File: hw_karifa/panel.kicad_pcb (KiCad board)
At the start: 2 copper layers, 141.8 x 210.4 mm, 763 parts, among them J1 Conn_2Rows-05Pins, Q1 AO3401A, Q2 AO3401A, Q3 AO3401A, SW1 SW_DPST_x2, U1 PY32F002AF15P6TU

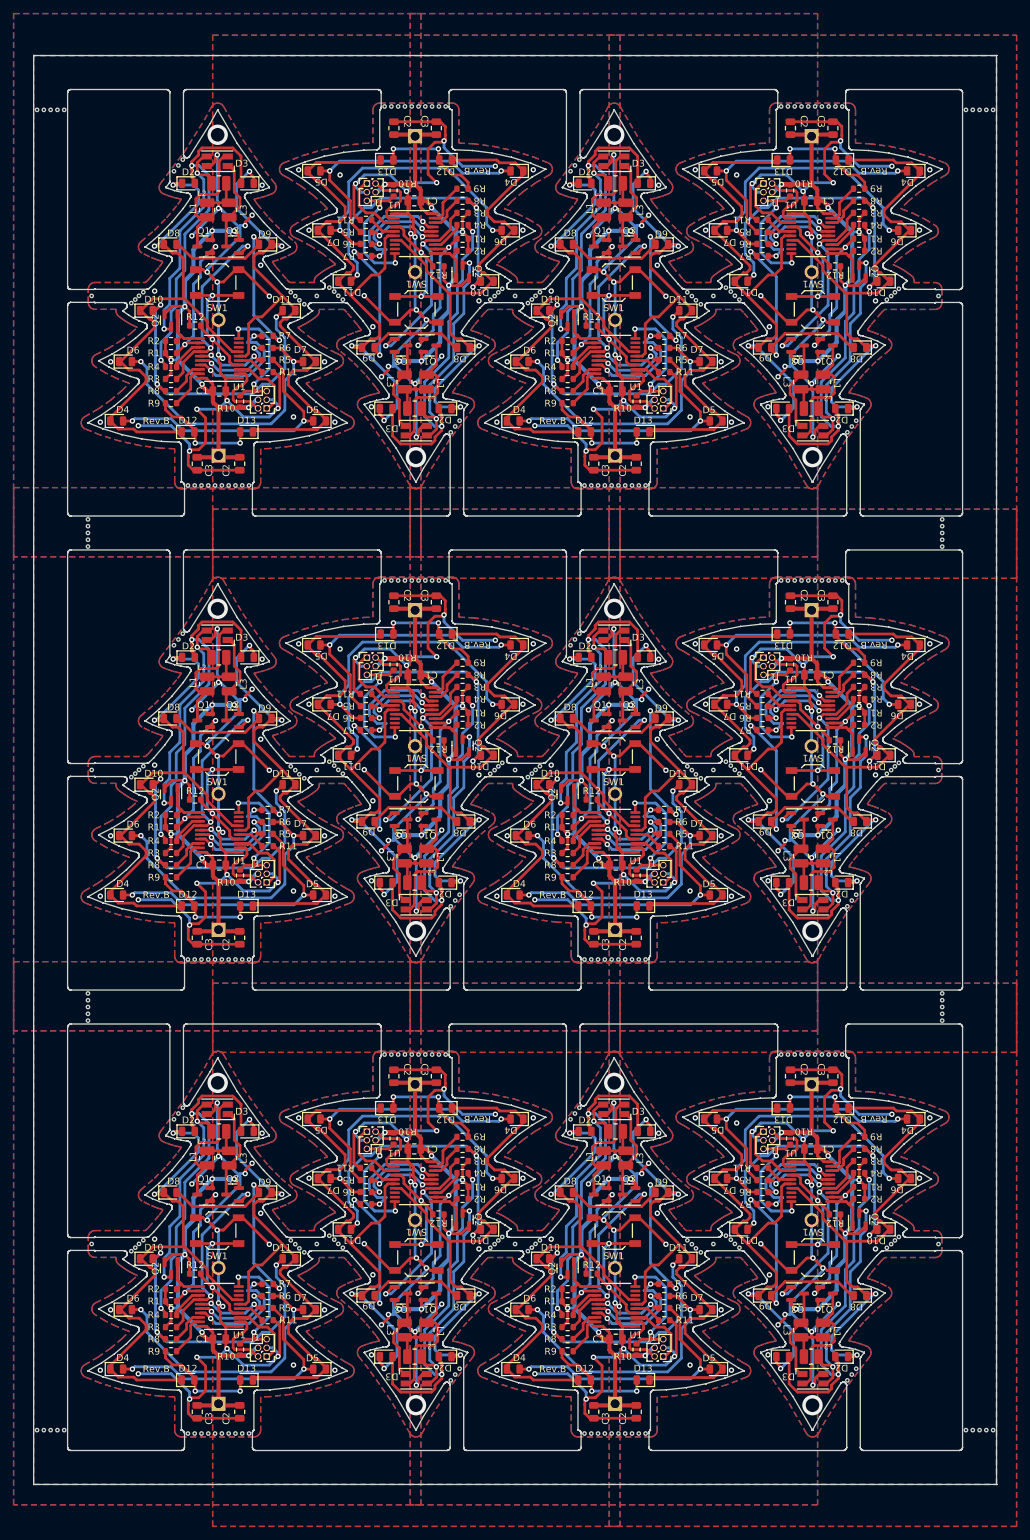
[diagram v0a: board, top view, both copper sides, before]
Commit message: Karifa updated and panelized.
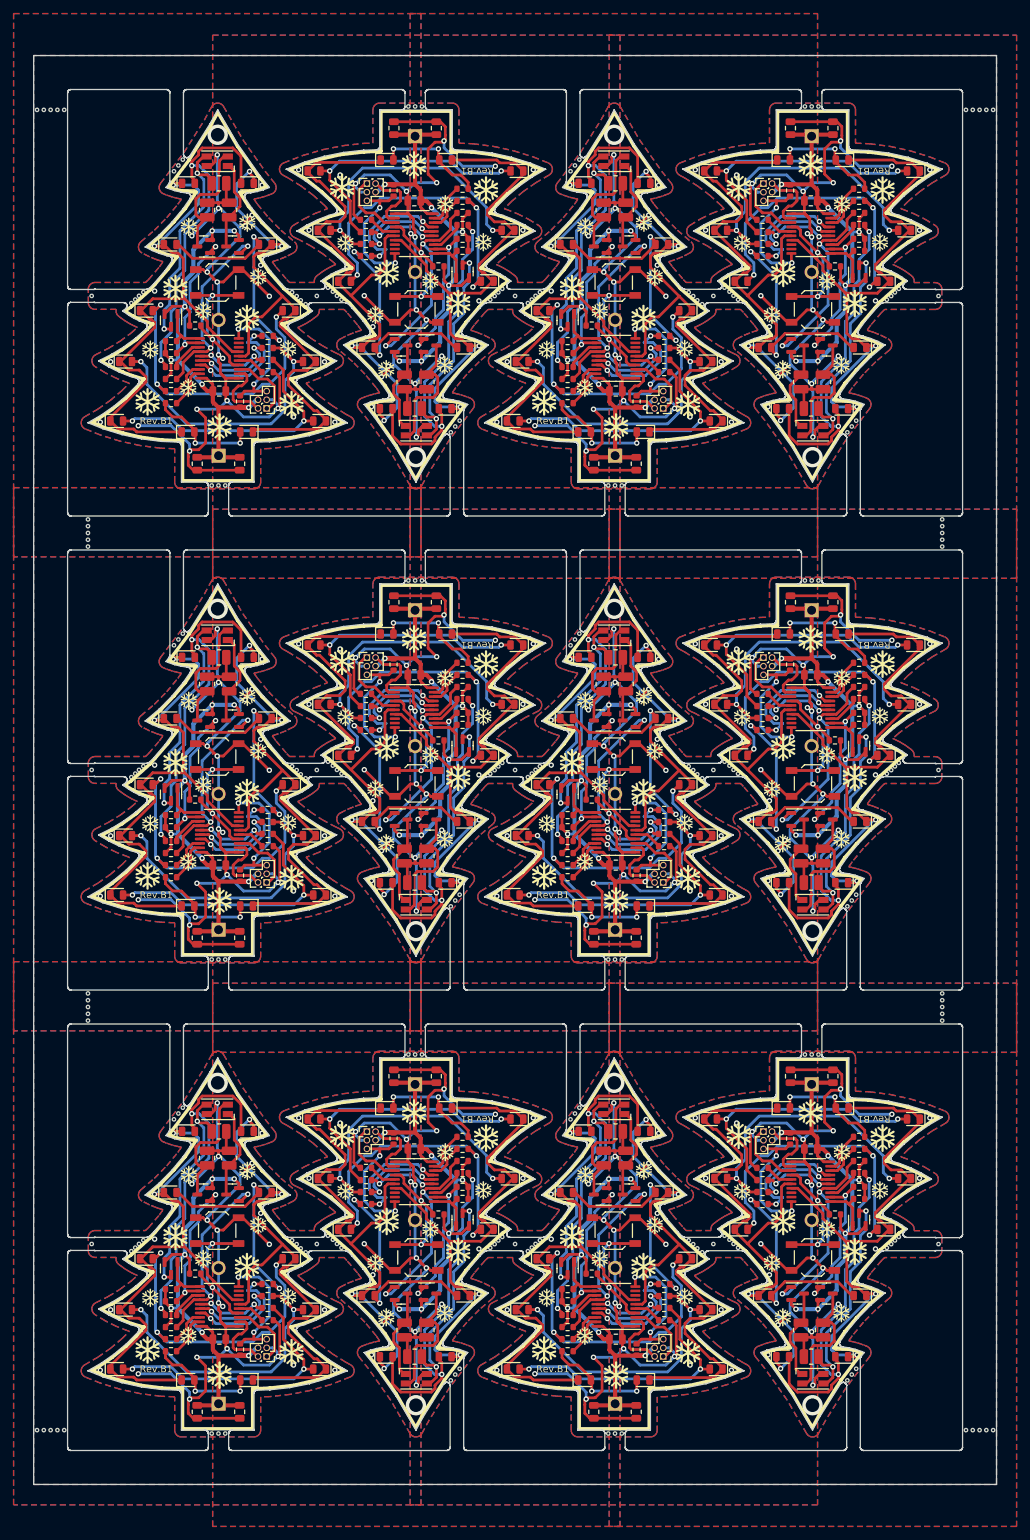
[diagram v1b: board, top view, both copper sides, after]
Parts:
- removed the ? at (117.5, 126.4)
- removed the ? at (179.5, 54.2)
- removed the ? at (179.5, 193.8)
- removed the ? at (121.1, 193.8)
- removed the ? at (121.1, 124.0)
- removed the ? at (179.5, 124.0)
- removed the ? at (117.5, 196.3)
- removed the ? at (175.9, 126.4)
- removed the ? at (121.1, 54.2)
- removed the ? at (117.5, 56.6)
- removed the ? at (175.9, 196.3)
- removed the ? at (175.9, 56.6)
- removed KiKit_MB_10_1, KiKit_MB_10_2, KiKit_MB_12_10, KiKit_MB_12_11, KiKit_MB_12_5, KiKit_MB_12_6, KiKit_MB_12_7, KiKit_MB_12_8, KiKit_MB_12_9, KiKit_MB_13_1, KiKit_MB_13_2, KiKit_MB_14_10, KiKit_MB_14_11, KiKit_MB_14_5, KiKit_MB_14_6, KiKit_MB_14_7, KiKit_MB_14_8, KiKit_MB_14_9, KiKit_MB_15_1, KiKit_MB_15_2, KiKit_MB_16_10, KiKit_MB_16_11, KiKit_MB_16_5, KiKit_MB_16_6, KiKit_MB_16_7, KiKit_MB_16_8, KiKit_MB_16_9, KiKit_MB_17_1, KiKit_MB_17_2, KiKit_MB_19_10, KiKit_MB_19_11, KiKit_MB_19_5, KiKit_MB_19_6, KiKit_MB_19_7, KiKit_MB_19_8, KiKit_MB_19_9, KiKit_MB_20_1, KiKit_MB_20_2, KiKit_MB_22_10, KiKit_MB_22_11, KiKit_MB_22_5, KiKit_MB_22_6, KiKit_MB_22_7, KiKit_MB_22_8, KiKit_MB_22_9, KiKit_MB_23_1, KiKit_MB_23_2, KiKit_MB_24_10, KiKit_MB_24_11, KiKit_MB_24_5, KiKit_MB_24_6, KiKit_MB_24_7, KiKit_MB_24_8, KiKit_MB_24_9, KiKit_MB_25_1, KiKit_MB_25_2, KiKit_MB_26_10, KiKit_MB_26_11, KiKit_MB_26_5, KiKit_MB_26_6, KiKit_MB_26_7, KiKit_MB_26_8, KiKit_MB_26_9, KiKit_MB_27_1, KiKit_MB_27_2, KiKit_MB_29_10, KiKit_MB_29_11, KiKit_MB_29_5, KiKit_MB_29_6, KiKit_MB_29_7, KiKit_MB_29_8, KiKit_MB_29_9, KiKit_MB_2_10, KiKit_MB_2_11, KiKit_MB_2_5, KiKit_MB_2_6, KiKit_MB_2_7, KiKit_MB_2_8, KiKit_MB_2_9, KiKit_MB_30_1, KiKit_MB_30_2, KiKit_MB_39_2, KiKit_MB_39_3, KiKit_MB_39_5, KiKit_MB_39_6, KiKit_MB_3_1, KiKit_MB_3_2, KiKit_MB_40_2, KiKit_MB_40_3, KiKit_MB_40_5, KiKit_MB_40_6, KiKit_MB_42_2, KiKit_MB_42_3, KiKit_MB_42_5, KiKit_MB_42_6, KiKit_MB_43_2, KiKit_MB_43_3, KiKit_MB_43_5, KiKit_MB_43_6, KiKit_MB_4_10, KiKit_MB_4_11, KiKit_MB_4_5, KiKit_MB_4_6, KiKit_MB_4_7, KiKit_MB_4_8, KiKit_MB_4_9, KiKit_MB_5_1, KiKit_MB_5_2, KiKit_MB_6_10, KiKit_MB_6_11, KiKit_MB_6_5, KiKit_MB_6_6, KiKit_MB_6_7, KiKit_MB_6_8, KiKit_MB_6_9, KiKit_MB_7_1, KiKit_MB_7_2, KiKit_MB_9_10, KiKit_MB_9_11, KiKit_MB_9_5, KiKit_MB_9_6, KiKit_MB_9_7, KiKit_MB_9_8, KiKit_MB_9_9: NPTH, NPTH
- removed the REF** at (121.9, 194.4)
- removed the REF** at (174.5, 55.4)
- removed the REF** at (173.9, 54.9)
- removed the REF** at (174.5, 125.2)
- removed the REF** at (181.5, 125.8)
- removed the REF** at (180.9, 195.0)
- removed the REF** at (180.9, 125.2)
- removed the REF** at (122.5, 55.4)
- removed the REF** at (115.5, 194.5)
- removed the REF** at (175.1, 125.9)
- removed the REF** at (174.5, 195.1)
- removed the REF** at (122.5, 195.0)
- removed the REF** at (116.1, 55.4)
- removed the REF** at (123.1, 125.8)
- removed the REF** at (181.5, 56.0)
- removed the REF** at (121.9, 124.6)
- removed the REF** at (116.1, 195.1)
- removed the REF** at (115.5, 54.9)
- removed the REF** at (116.7, 125.9)
- removed the REF** at (173.9, 124.7)
- removed the REF** at (175.1, 195.7)
- removed the REF** at (115.5, 124.7)
- removed the REF** at (123.1, 56.0)
- removed the REF** at (121.9, 54.8)
- removed the REF** at (116.7, 56.0)
- removed the REF** at (116.1, 125.2)
- removed the REF** at (181.5, 195.6)
- removed the REF** at (180.3, 124.6)
- removed the REF** at (180.9, 55.4)
- removed the REF** at (175.1, 56.0)
- removed the REF** at (123.1, 195.6)
- removed the REF** at (173.9, 194.5)
- removed the REF** at (116.7, 195.7)
- removed the REF** at (180.3, 194.4)
- removed the REF** at (122.5, 125.2)
- removed the REF** at (180.3, 54.8)
- added ?: , , F.Cu at (176.1, 196.3)
- added ?: , , F.Cu at (176.1, 56.6)
- added ?: , , F.Cu at (179.3, 124.0)
- added ?: , , F.Cu at (176.1, 126.4)
- added ?: , , F.Cu at (117.7, 56.6)
- added ?: , , F.Cu at (179.3, 54.2)
- added ?: , , F.Cu at (120.9, 54.2)
- added ?: , , F.Cu at (117.7, 196.3)
- added ?: , , F.Cu at (120.9, 124.0)
- added ?: , , F.Cu at (179.3, 193.8)
- added ?: , , F.Cu at (117.7, 126.4)
- added ?: , , F.Cu at (120.9, 193.8)
- added KiKit_MB_10_4: NPTH, NPTH, F.Cu at (198.1, 74.6)
- added KiKit_MB_10_5: NPTH, NPTH, F.Cu at (197.4, 75.5)
- added KiKit_MB_13_4: NPTH, NPTH, F.Cu at (98.9, 106.0)
- added KiKit_MB_13_5: NPTH, NPTH, F.Cu at (99.6, 105.1)
- added KiKit_MB_15_4: NPTH, NPTH, F.Cu at (139.7, 144.4)
- added KiKit_MB_15_5: NPTH, NPTH, F.Cu at (139.0, 145.3)
- added KiKit_MB_17_4: NPTH, NPTH, F.Cu at (157.3, 106.0)
- added KiKit_MB_17_5: NPTH, NPTH, F.Cu at (158.0, 105.1)
- added KiKit_MB_20_4: NPTH, NPTH, F.Cu at (198.1, 144.4)
- added KiKit_MB_20_5: NPTH, NPTH, F.Cu at (197.4, 145.3)
- added KiKit_MB_23_4: NPTH, NPTH, F.Cu at (98.9, 175.8)
- added KiKit_MB_23_5: NPTH, NPTH, F.Cu at (99.6, 175.0)
- added KiKit_MB_25_4: NPTH, NPTH, F.Cu at (139.7, 214.3)
- added KiKit_MB_25_5: NPTH, NPTH, F.Cu at (139.0, 215.1)
- added KiKit_MB_27_4: NPTH, NPTH, F.Cu at (157.3, 175.8)
- added KiKit_MB_27_5: NPTH, NPTH, F.Cu at (158.0, 175.0)
- added KiKit_MB_30_4: NPTH, NPTH, F.Cu at (198.1, 214.3)
- added KiKit_MB_30_5: NPTH, NPTH, F.Cu at (197.4, 215.1)
- added KiKit_MB_31_2: NPTH, NPTH, F.Cu at (85.6, 88.3)
- added KiKit_MB_31_3: NPTH, NPTH, F.Cu at (85.6, 89.3)
- added KiKit_MB_31_5: NPTH, NPTH, F.Cu at (85.6, 91.3)
- added KiKit_MB_31_6: NPTH, NPTH, F.Cu at (85.6, 92.3)
- added KiKit_MB_32_2: NPTH, NPTH, F.Cu at (211.4, 88.3)
- added KiKit_MB_32_3: NPTH, NPTH, F.Cu at (211.4, 89.3)
- added KiKit_MB_32_5: NPTH, NPTH, F.Cu at (211.4, 91.3)
- added KiKit_MB_32_6: NPTH, NPTH, F.Cu at (211.4, 92.3)
- added KiKit_MB_33_2: NPTH, NPTH, F.Cu at (85.6, 158.1)
- added KiKit_MB_33_3: NPTH, NPTH, F.Cu at (85.6, 159.1)
- added KiKit_MB_33_5: NPTH, NPTH, F.Cu at (85.6, 161.1)
- added KiKit_MB_33_6: NPTH, NPTH, F.Cu at (85.6, 162.1)
- added KiKit_MB_34_2: NPTH, NPTH, F.Cu at (211.4, 158.1)
- added KiKit_MB_34_3: NPTH, NPTH, F.Cu at (211.4, 159.1)
- added KiKit_MB_34_5: NPTH, NPTH, F.Cu at (211.4, 161.1)
- added KiKit_MB_34_6: NPTH, NPTH, F.Cu at (211.4, 162.1)
- added KiKit_MB_3_4: NPTH, NPTH, F.Cu at (98.9, 36.2)
- added KiKit_MB_3_5: NPTH, NPTH, F.Cu at (99.6, 35.3)
- added KiKit_MB_5_4: NPTH, NPTH, F.Cu at (139.7, 74.6)
- added KiKit_MB_5_5: NPTH, NPTH, F.Cu at (139.0, 75.5)
- added KiKit_MB_7_4: NPTH, NPTH, F.Cu at (157.3, 36.2)
- added KiKit_MB_7_5: NPTH, NPTH, F.Cu at (158.0, 35.3)
- added REF**: NPTH, NPTH, F.Cu at (180.7, 125.2)
- added REF**: NPTH, NPTH, F.Cu at (174.7, 125.2)
- added REF**: NPTH, NPTH, F.Cu at (122.3, 125.2)
- added REF**: NPTH, NPTH, F.Cu at (181.3, 125.8)
- added REF**: NPTH, NPTH, F.Cu at (175.3, 195.7)
- added REF**: NPTH, NPTH, F.Cu at (174.7, 55.4)
- added REF**: NPTH, NPTH, F.Cu at (174.1, 194.5)
- added REF**: NPTH, NPTH, F.Cu at (121.7, 54.8)
- added REF**: NPTH, NPTH, F.Cu at (122.9, 195.6)
- added REF**: NPTH, NPTH, F.Cu at (174.1, 124.7)
- added REF**: NPTH, NPTH, F.Cu at (116.9, 125.9)
- added REF**: NPTH, NPTH, F.Cu at (175.3, 56.0)
- added REF**: NPTH, NPTH, F.Cu at (175.3, 125.9)
- added REF**: NPTH, NPTH, F.Cu at (115.7, 124.7)
- added REF**: NPTH, NPTH, F.Cu at (116.9, 195.7)
- added REF**: NPTH, NPTH, F.Cu at (116.3, 125.2)
- added REF**: NPTH, NPTH, F.Cu at (174.1, 54.9)
- added REF**: NPTH, NPTH, F.Cu at (180.1, 194.4)
- added REF**: NPTH, NPTH, F.Cu at (116.3, 195.1)
- added REF**: NPTH, NPTH, F.Cu at (122.3, 55.4)
- added REF**: NPTH, NPTH, F.Cu at (122.9, 125.8)
- added REF**: NPTH, NPTH, F.Cu at (180.7, 195.0)
- added REF**: NPTH, NPTH, F.Cu at (174.7, 195.1)
- added REF**: NPTH, NPTH, F.Cu at (180.1, 124.6)
- added REF**: NPTH, NPTH, F.Cu at (115.7, 54.9)
- added REF**: NPTH, NPTH, F.Cu at (121.7, 194.4)
- added REF**: NPTH, NPTH, F.Cu at (122.9, 56.0)
- added REF**: NPTH, NPTH, F.Cu at (116.3, 55.4)
- added REF**: NPTH, NPTH, F.Cu at (115.7, 194.5)
- added REF**: NPTH, NPTH, F.Cu at (181.3, 195.6)
- added REF**: NPTH, NPTH, F.Cu at (121.7, 124.6)
- added REF**: NPTH, NPTH, F.Cu at (181.3, 56.0)
- added REF**: NPTH, NPTH, F.Cu at (116.9, 56.0)
- added REF**: NPTH, NPTH, F.Cu at (180.1, 54.8)
- added REF**: NPTH, NPTH, F.Cu at (180.7, 55.4)
- added REF**: NPTH, NPTH, F.Cu at (122.3, 195.0)
- moved KiKit_MB_37_4 139.6 mm to (148.5, 55.4)
- moved KiKit_MB_31_4 139.5 mm to (85.6, 90.3)
- moved KiKit_MB_33_4 110.0 mm to (85.6, 160.1)
- moved KiKit_MB_34_4 110.0 mm to (211.4, 160.1)
- moved KiKit_MB_32_4 98.5 mm to (211.4, 90.3)
- moved KiKit_MB_42_4 98.5 mm to (177.7, 125.2)
- moved KiKit_MB_35_4 75.7 mm to (119.3, 195.0)
- moved KiKit_MB_43_4 71.9 mm to (148.5, 195.0)
- moved KiKit_MB_41_4 69.8 mm to (148.5, 125.2)
- moved KiKit_MB_36_4 69.8 mm to (177.7, 195.0)
- moved KiKit_MB_38_4 69.8 mm to (119.3, 125.2)
- moved KiKit_MB_39_4 48.5 mm to (119.3, 55.4)
- moved KiKit_MB_40_4 48.5 mm to (177.7, 55.4)
- moved KiKit_MB_12_2 5.50 mm to (105.8, 153.1)
- moved KiKit_MB_14_2 5.50 mm to (132.8, 97.3)
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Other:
- outline, holes or cut-outs redrawn
- board text added: "Rev.B1"
- board text removed: "Rev.B"
